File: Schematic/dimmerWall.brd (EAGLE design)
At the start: 51.4 x 51.1 mm, 22 parts, among them Q1 IRF840, T1 BC547

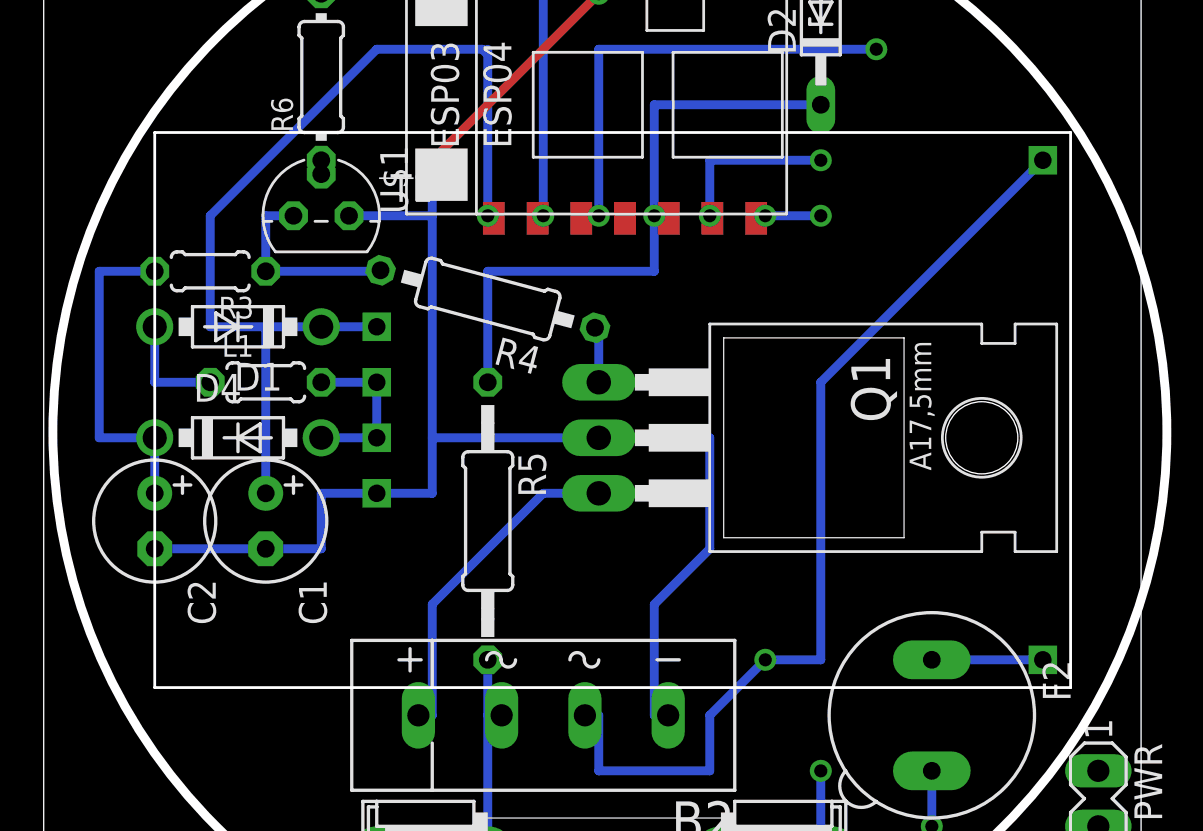
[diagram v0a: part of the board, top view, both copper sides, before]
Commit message: Add SMPS with correct dimmensions
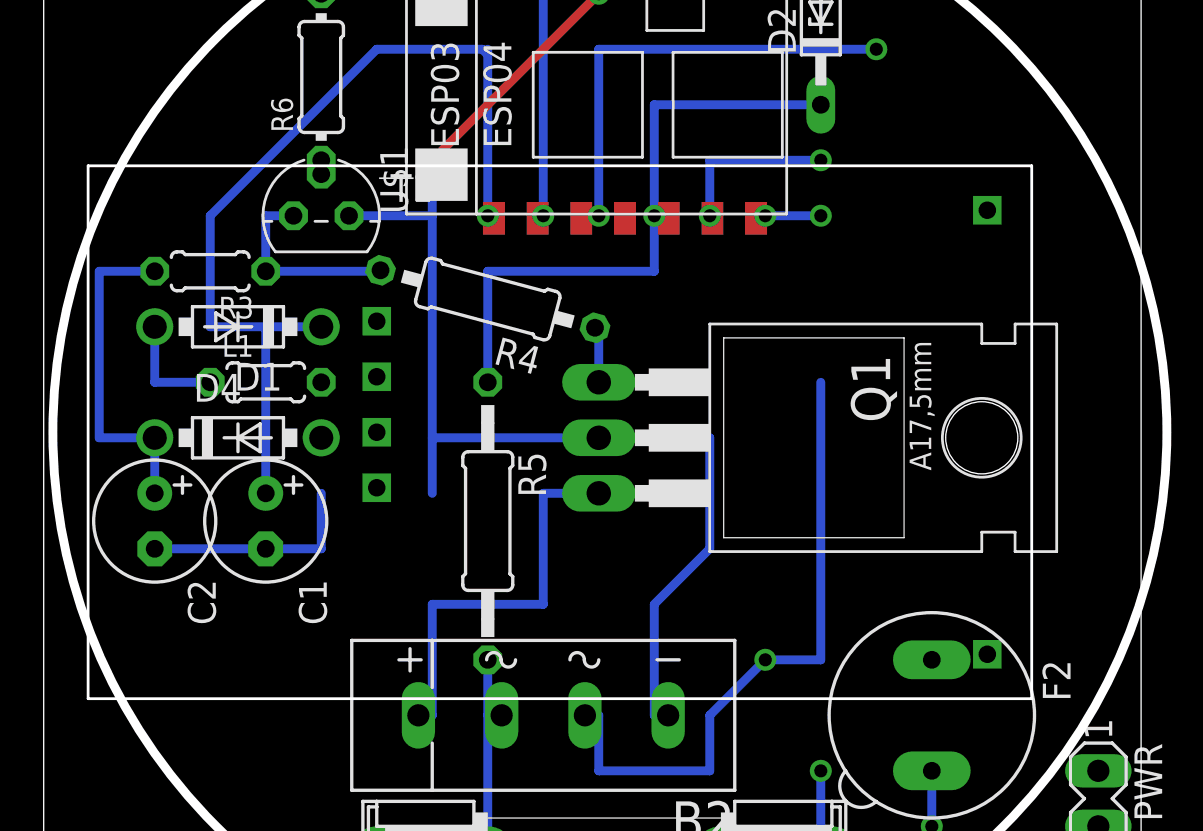
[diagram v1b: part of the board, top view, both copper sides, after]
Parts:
- moved U$2 28.5 mm to (22.9, 25.7)
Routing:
- net N$4: track 44.2 -> 29.9 mm
- net N$6: track 7.62 -> 0.00 mm
- net GND: track 88.0 -> 83.0 mm
- net N$9: track 5.08 -> 0.00 mm
- net N$21: track 15.4 -> 18.4 mm
- net +3V3: track 44.3 -> 41.8 mm
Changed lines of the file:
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@@
 <element name="U$1" library="esp8266modules" package="ESP-03" value="ESP8266" x="25.4" y="40.64" rot="R90"/>
 <element name="T1" library="transistor" package="TO92" value="BC547" x="12.7" y="35.56"/>
-<element name="U$2" library="smps" package="SMPS" value="SMPS" x="48.26" y="12.7" rot="R180"/>
 <element name="D1" library="diode" package="DO41-7.6" value="1N5817-B" x="8.89" y="30.48" rot="R180"/>
 <element name="D4" library="diode" package="DO41-7.6" value="1N5817-B" x="8.89" y="25.4"/>
@@
 <attribute name="OC_FARNELL" value="176432" x="60.96" y="36.068" size="1.778" layer="27" rot="R90" display="off"/>
 </element>
+<element name="U$2" library="smps" package="SMPS" value="SMPS" x="22.86" y="25.654" rot="R180"/>
 </elements>
 <signals>
@@
 <contactref element="C1" pad="+"/>
 <contactref element="U$1" pad="VCC"/>
-<contactref element="U$2" pad="FB"/>
 <contactref element="D1" pad="C"/>
-<wire x1="15.24" y1="30.48" x2="12.7" y2="30.48" width="0.4064" layer="16"/>
 <wire x1="10.16" y1="22.86" x2="10.16" y2="30.48" width="0.4064" layer="16"/>
 <wire x1="10.16" y1="30.48" x2="12.7" y2="30.48" width="0.4064" layer="16"/>
@@
 <wire x1="15.24" y1="43.18" x2="20.066" y2="43.18" width="0.4064" layer="16"/>
 <wire x1="20.066" y1="43.18" x2="20.32" y2="42.926" width="0.4064" layer="16"/>
+<contactref element="U$2" pad="FB"/>
+<wire x1="15.24" y1="30.734" x2="10.16" y2="22.86" width="0" layer="19" extent="1-1"/>
 </signal>
 <signal name="GND">
@@
 <contactref element="Q1" pad="2"/>
 <contactref element="T1" pad="1"/>
-<contactref element="U$2" pad="GND"/>
 <wire x1="5.08" y1="20.32" x2="10.16" y2="20.32" width="0.4064" layer="16"/>
 <wire x1="25.4" y1="25.4" x2="17.78" y2="25.4" width="0.4064" layer="16"/>
 <wire x1="17.78" y1="25.4" x2="17.78" y2="22.86" width="0.4064" layer="16"/>
-<wire x1="17.78" y1="22.86" x2="15.24" y2="22.86" width="0.4064" layer="16"/>
 <wire x1="13.97" y1="35.56" x2="17.78" y2="35.56" width="0.4064" layer="16"/>
 <wire x1="17.78" y1="35.56" x2="17.78" y2="38.1" width="0.4064" layer="16"/>
@@
 <wire x1="10.16" y1="20.32" x2="12.7" y2="20.32" width="0.4064" layer="16"/>
 <wire x1="12.7" y1="20.32" x2="12.7" y2="22.86" width="0.4064" layer="16"/>
-<wire x1="12.7" y1="22.86" x2="15.24" y2="22.86" width="0.4064" layer="16"/>
 <wire x1="28.575" y1="12.7" x2="27.94" y2="12.7" width="0.4064" layer="16"/>
 <wire x1="27.94" y1="12.7" x2="27.94" y2="17.78" width="0.4064" layer="16"/>
@@
 <contactref element="S1" pad="3"/>
 <contactref element="S1" pad="4"/>
+<contactref element="U$2" pad="GND"/>
 <wire x1="63.2206" y1="44.2468" x2="63.2206" y2="50.7492" width="0" layer="19" extent="1-1"/>
 <wire x1="63.2206" y1="39.3192" x2="63.2206" y2="44.2468" width="0" layer="19" extent="1-1"/>
@@
 <wire x1="63.2206" y1="12.2428" x2="63.2206" y2="18.7452" width="0" layer="19" extent="1-1"/>
 <wire x1="35.56" y1="45.72" x2="63.2206" y2="44.2468" width="0" layer="19" extent="16-16"/>
+<wire x1="12.7" y1="22.86" x2="17.78" y2="22.86" width="0" layer="19" extent="16-16"/>
+<wire x1="15.24" y1="23.114" x2="28.575" y2="12.7" width="0" layer="19" extent="1-1"/>
 </signal>
 <signal name="N$17">
@@
 <wire x1="17.145" y1="12.7" x2="17.78" y2="12.7" width="0.4064" layer="16"/>
 <wire x1="25.4" y1="22.86" x2="22.86" y2="22.86" width="0.4064" layer="16"/>
-<wire x1="22.86" y1="22.86" x2="17.78" y2="17.78" width="0.4064" layer="16"/>
+<wire x1="22.86" y1="22.86" x2="22.86" y2="17.78" width="0.4064" layer="16"/>
+<wire x1="22.86" y1="17.78" x2="17.78" y2="17.78" width="0.4064" layer="16"/>
 <wire x1="17.78" y1="17.78" x2="17.78" y2="12.7" width="0.4064" layer="16"/>
 </signal>
@@
 <contactref element="F2" pad="1"/>
 <contactref element="U$2" pad="L"/>
-<wire x1="45.72" y1="15.24" x2="40.64" y2="15.24" width="0.4064" layer="16"/>
+<wire x1="43.18" y1="15.494" x2="40.64" y2="15.24" width="0" layer="19" extent="1-1"/>
 </signal>
 <signal name="N$12">
@@
 <signal name="N$6">
 <contactref element="L1" pad="2"/>
+<contactref element="D4" pad="A"/>
+<contactref element="U$2" pad="VPP1"/>
 <contactref element="U$2" pad="VPP2"/>
-<contactref element="U$2" pad="VPP1"/>
-<contactref element="D4" pad="A"/>
-<wire x1="12.7" y1="27.94" x2="15.24" y2="27.94" width="0.4064" layer="16"/>
-<wire x1="12.7" y1="25.4" x2="15.24" y2="25.4" width="0.4064" layer="16"/>
-<wire x1="15.24" y1="25.4" x2="15.24" y2="27.94" width="0.4064" layer="16"/>
+<wire x1="12.7" y1="25.4" x2="12.7" y2="27.94" width="0" layer="19" extent="1-1"/>
+<wire x1="15.24" y1="25.654" x2="12.7" y2="25.4" width="0" layer="19" extent="1-1"/>
+<wire x1="15.24" y1="28.194" x2="15.24" y2="25.654" width="0" layer="19" extent="1-1"/>
 </signal>
 <signal name="+5V">
@@
 <signal name="N$4">
 <contactref element="PWR" pad="1"/>
-<contactref element="U$2" pad="N"/>
 <contactref element="B2" pad="AC1"/>
 <wire x1="24.765" y1="12.7" x2="25.4" y2="12.7" width="0.4064" layer="16"/>
@@
 <via x="33.02" y="15.24" extent="1-16" drill="0.6" shape="square"/>
 <wire x1="33.02" y1="15.24" x2="33.274" y2="15.24" width="0.4064" layer="1"/>
-<wire x1="45.72" y1="38.1" x2="35.56" y2="27.94" width="0.4064" layer="16"/>
 <wire x1="35.56" y1="27.94" x2="35.56" y2="15.24" width="0.4064" layer="16"/>
 <wire x1="35.56" y1="15.24" x2="33.02" y2="15.24" width="0.4064" layer="16"/>
+<contactref element="U$2" pad="N"/>
 <wire x1="35.56" y1="15.24" x2="48.26" y2="10.16" width="0" layer="19" extent="16-16"/>
+<wire x1="43.18" y1="35.814" x2="25.4" y2="10.16" width="0" layer="19" extent="16-16"/>
 </signal>
 <signal name="N$5">

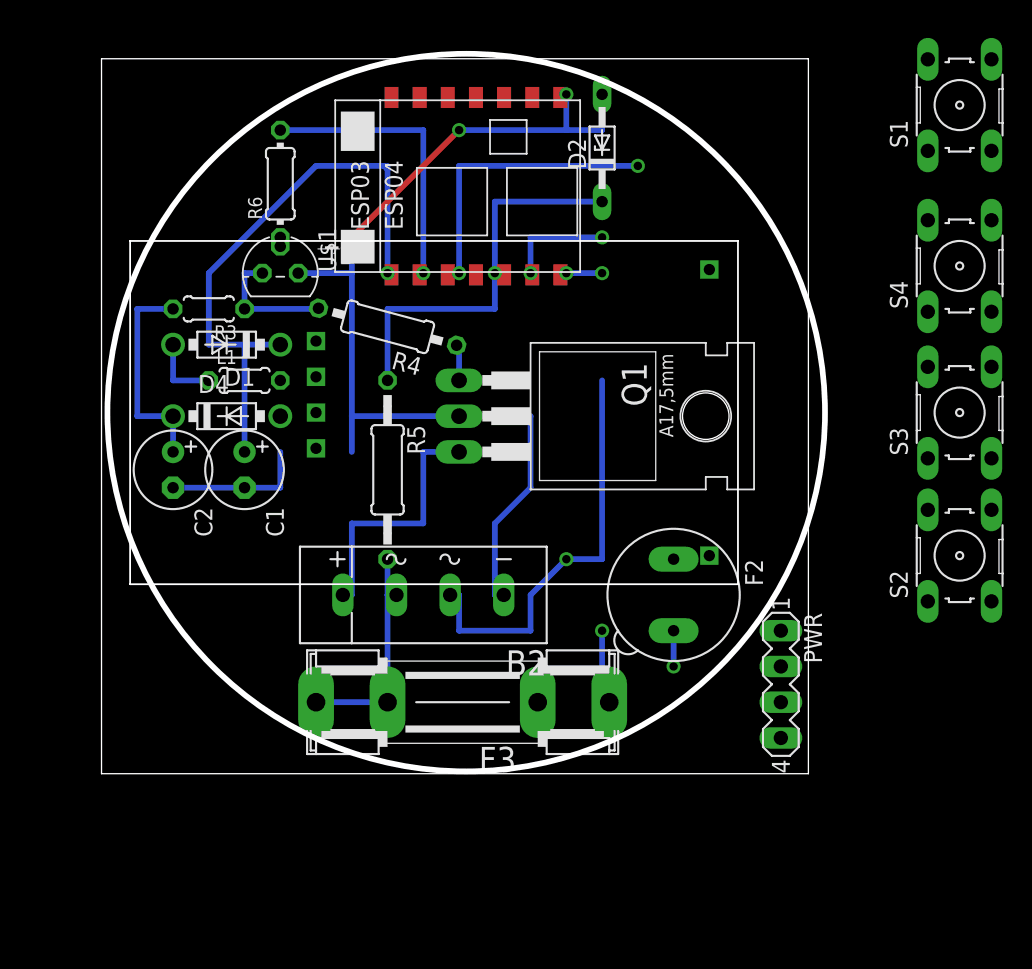
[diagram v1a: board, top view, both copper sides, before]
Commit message: Add L dimension
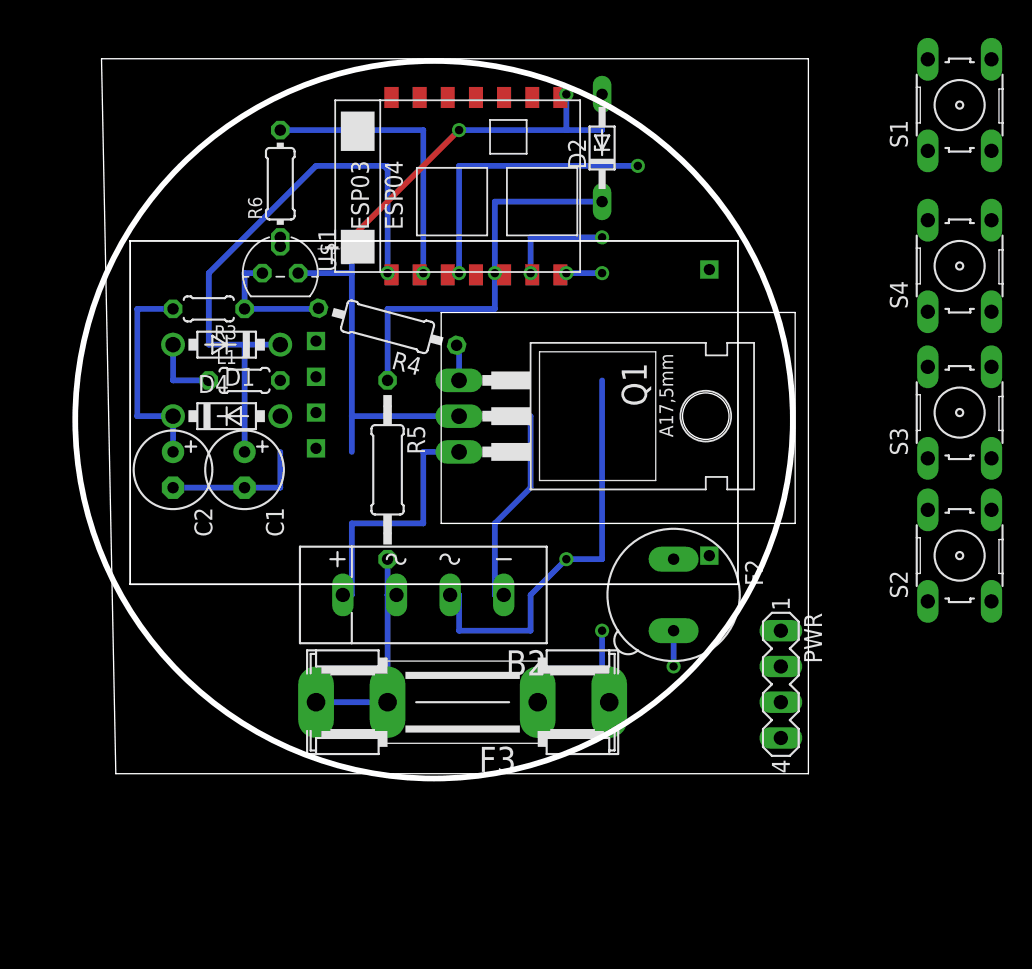
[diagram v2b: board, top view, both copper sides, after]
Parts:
- D4: value 1N5817-B -> 1N4148
- L1: value (none) -> 330n
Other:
- board size 51.4 x 51.1 mm -> 52.1 x 51.1 mm
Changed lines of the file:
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@@
 <setting verticaltext="up"/>
 </settings>
-<grid distance="0.01" unitdist="inch" unit="inch" style="lines" multiple="10" display="yes" altdistance="0.025" altunitdist="inch" altunit="inch"/>
+<grid distance="0.01" unitdist="inch" unit="mm" style="lines" multiple="10" display="yes" altdistance="0.025" altunitdist="inch" altunit="inch"/>
 <layers>
 <layer number="1" name="Top" color="4" fill="1" visible="yes" active="yes"/>
@@
 <layer number="45" name="Holes" color="7" fill="1" visible="no" active="yes"/>
 <layer number="46" name="Milling" color="3" fill="1" visible="no" active="yes"/>
-<layer number="47" name="Measures" color="7" fill="1" visible="no" active="yes"/>
+<layer number="47" name="Measures" color="7" fill="1" visible="yes" active="yes"/>
 <layer number="48" name="Document" color="7" fill="1" visible="yes" active="yes"/>
 <layer number="49" name="Reference" color="7" fill="1" visible="yes" active="yes"/>
@@
 <board>
 <plain>
-<wire x1="0" y1="0" x2="50.216" y2="0" width="0" layer="20"/>
+<wire x1="1.016" y1="0" x2="50.216" y2="0" width="0" layer="20"/>
 <wire x1="50.216" y1="0" x2="50.216" y2="50.79" width="0" layer="20"/>
 <wire x1="50.216" y1="50.79" x2="0" y2="50.79" width="0" layer="20"/>
-<wire x1="0" y1="50.79" x2="0" y2="0" width="0" layer="20"/>
-<circle x="25.908" y="25.654" radius="25.487478125" width="0.4064" layer="20"/>
+<wire x1="0" y1="50.79" x2="1.016" y2="0" width="0" layer="20"/>
+<circle x="23.622" y="25.146" radius="25.487478125" width="0.4064" layer="20"/>
+<rectangle x1="24.13" y1="17.78" x2="49.276" y2="32.766" layer="20"/>
 </plain>
 <attributes>
@@
 <element name="C1" library="rcl" package="E2,5-6" value="10u/16" x="10.16" y="21.59" rot="R270"/>
 <element name="C2" library="rcl" package="E2,5-6" value="10u/16" x="5.08" y="21.59" rot="R270"/>
-<element name="L1" library="rcl" package="0204/5" value="" x="10.16" y="27.94"/>
+<element name="L1" library="rcl" package="0204/5" value="330n" x="10.16" y="27.94"/>
 <element name="U$1" library="esp8266modules" package="ESP-03" value="ESP8266" x="25.4" y="40.64" rot="R90"/>
 <element name="T1" library="transistor" package="TO92" value="BC547" x="12.7" y="35.56"/>
 <element name="D1" library="diode" package="DO41-7.6" value="1N5817-B" x="8.89" y="30.48" rot="R180"/>
-<element name="D4" library="diode" package="DO41-7.6" value="1N5817-B" x="8.89" y="25.4"/>
+<element name="D4" library="diode" package="DO41-7.6" value="1N4148" x="8.89" y="25.4"/>
 <element name="F3" library="fuse" package="SHK20L" value="1A flink" x="25.654" y="5.08" rot="R180">
 <attribute name="MF" value="" x="25.654" y="5.08" size="1.778" layer="27" rot="R180" display="off"/>

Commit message: Make board less higher
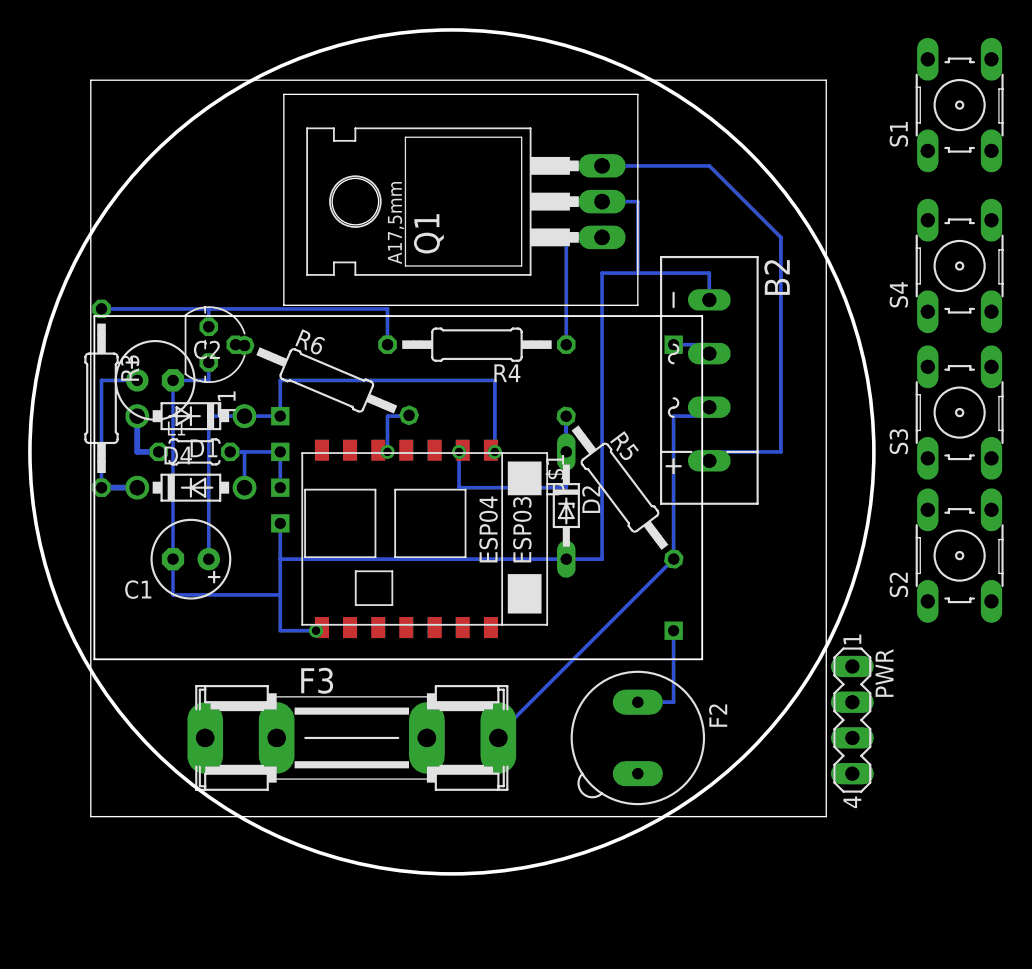
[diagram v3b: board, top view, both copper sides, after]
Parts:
- R3: device rcl:0204/5 -> rcl:0207/12
- R4: device rcl:0207/10 -> rcl:0207/12
- R5: value 1M -> 1M8
- R6: value 680 -> 51k; device rcl:0204/7 -> rcl:0207/12
- moved D2 25.5 mm to (33.0, 19.1), turned to 270 degrees
- moved B2 25.4 mm to (43.2, 27.9), turned to 270 degrees
- moved U$1 23.0 mm to (22.9, 17.8), turned to 270 degrees
- moved R5 16.6 mm to (36.8, 20.3), turned to 307 degrees
- moved Q1 15.5 mm to (29.2, 40.6), turned to 90 degrees
- moved R6 14.4 mm to (16.0, 27.9), turned to 337 degrees
- moved F2 10.5 mm to (38.1, 2.54)
- moved R3 9.92 mm to (0.00, 26.7), turned to 270 degrees
- moved F3 8.27 mm to (17.8, 2.54), turned to 0 degrees
- moved C1 7.41 mm to (6.35, 15.2), turned to 180 degrees
- moved T1 7.18 mm to (7.62, 30.5), turned to 270 degrees
- moved C2 6.48 mm to (3.81, 27.9), turned to 0 degrees
- moved R4 6.48 mm to (26.7, 30.5), turned to 180 degrees
- moved L1 6.20 mm to (6.60, 22.9)
- moved U$2 5.91 mm to (20.3, 20.3)
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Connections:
- removed net N$12: R6.2, U$1.GPIO14
- new net N$10: R6.2, U$1.GPIO15
- net N$7: now also U$1.GPIO14; no longer U$1.GPIO15
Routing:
- net N$4: track 29.9 -> 3.18 mm, vias 1 -> 0
- net N$16: track 21.4 -> 0.00 mm, vias 2 -> 0
- net N$12: track 20.7 -> 0.00 mm, vias 1 -> 0
- net N$21: track 18.4 -> 35.8 mm
- net N$17: track 15.9 -> 31.6 mm
- net N$2: track 9.07 -> 24.1 mm
- net GND: track 83.0 -> 97.8 mm, vias 3 -> 1
- net N$7: track 28.7 -> 18.3 mm
- net N$6: track 0.00 -> 9.65 mm
- net N$14: track 8.04 -> 0.00 mm, vias 2 -> 0
- net N$9: track 0.00 -> 7.62 mm
- net N$1: track 2.67 -> 10.2 mm
- net N$31: track 5.84 -> 0.00 mm, vias 1 -> 0
- net N$10: track 0.00 -> 4.97 mm, vias 0 -> 1
- net N$13: track 3.26 -> 0.00 mm, vias 2 -> 0
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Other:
- board size 52.1 x 51.1 mm -> 60 x 60 mm
